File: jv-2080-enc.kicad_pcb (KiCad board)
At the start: 2 copper layers, 40 x 30 mm, 9 parts, among them J1 Conn_01x04, SW1 RotaryEncoder_Switch, U1 ATtiny13A-P

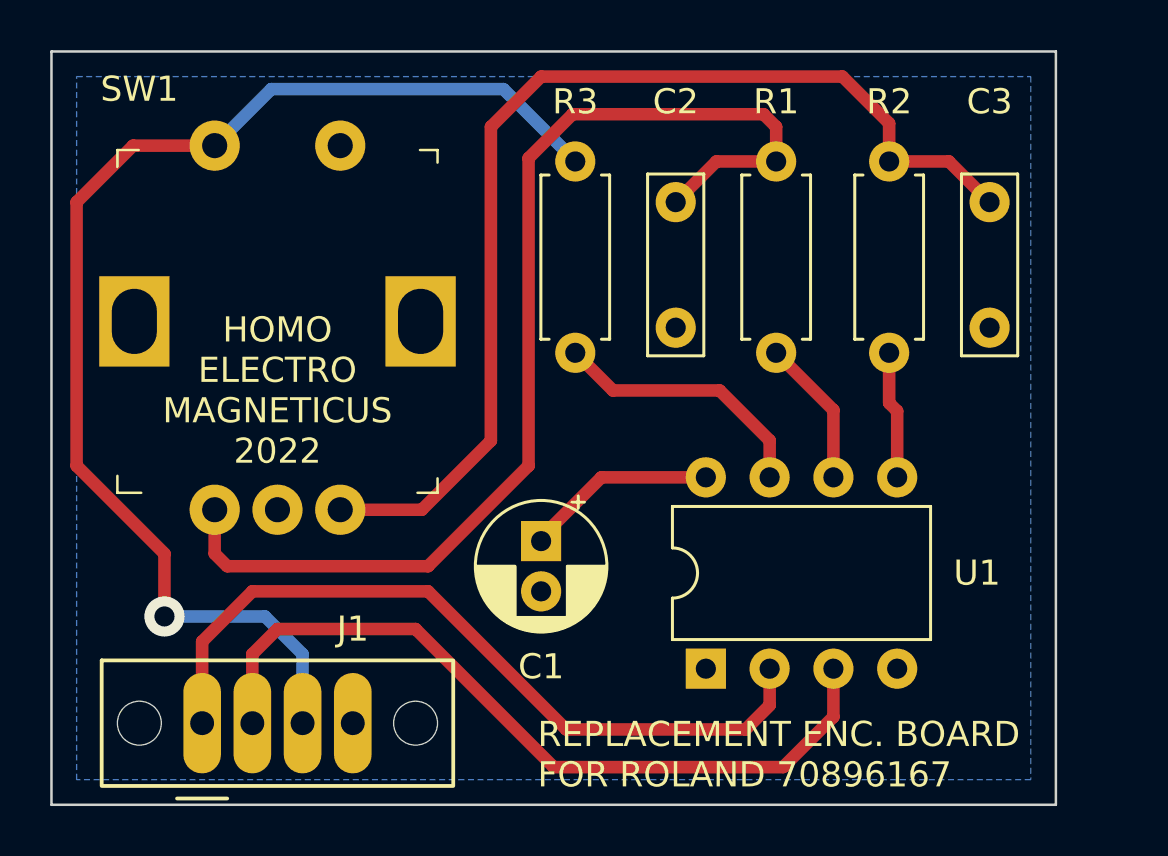
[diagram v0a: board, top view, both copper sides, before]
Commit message: Rounding all the tracks and adding teardrops for fun.
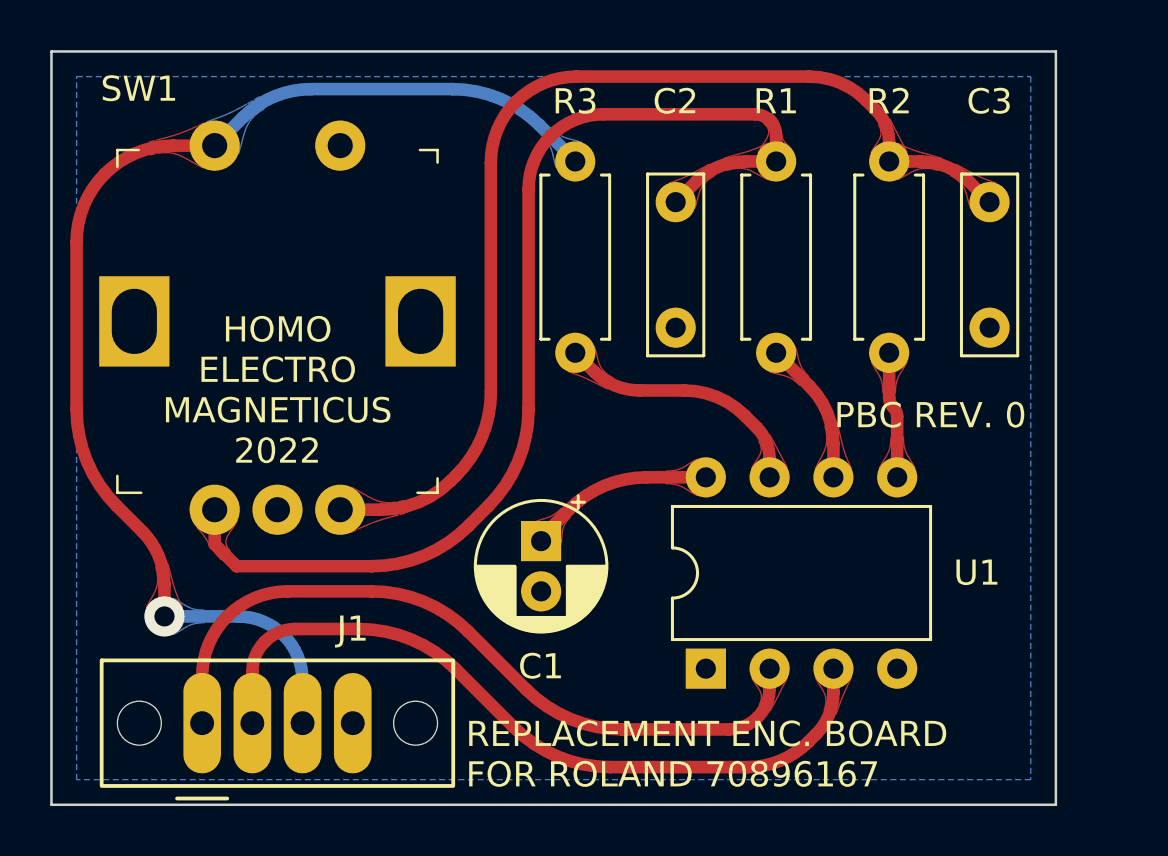
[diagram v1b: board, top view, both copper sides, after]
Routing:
- net Net-(C2-Pad1): track 45.5 -> 43.8 mm
- net Net-(C3-Pad1): track 43.3 -> 41.8 mm
- net /SWITCH: track 49.7 -> 48.3 mm
- net /ENC_A_OUT: track 30.8 -> 29.8 mm
- net /ENC_B_OUT: track 31.3 -> 30.4 mm
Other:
- board text added: "PBC REV. 0"

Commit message: Moved most of the components to the other side of the PCBA to account for the much smaller body size of a modern encoder vs the original one.
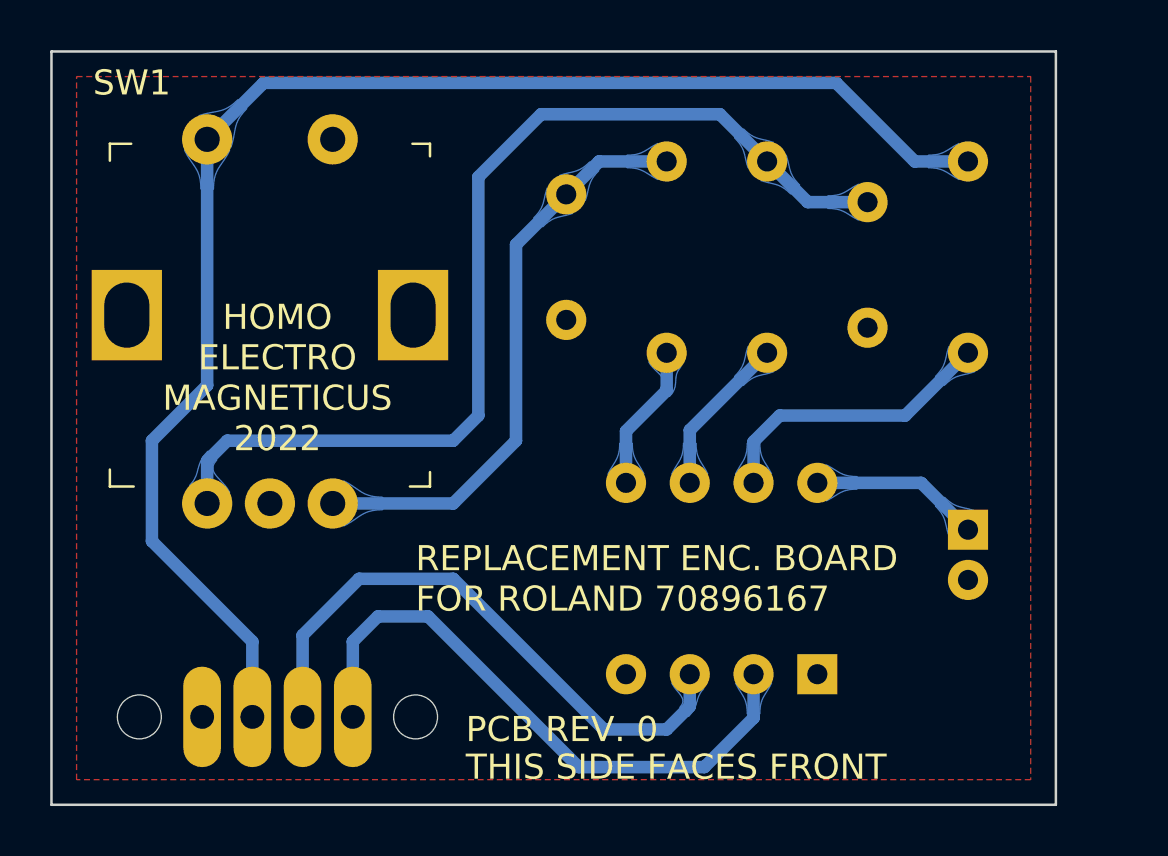
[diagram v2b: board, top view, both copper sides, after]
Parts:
- C1, C2, C3, J1, R1, R2, R3, U1: moved to B.Cu
- moved C1 17.0 mm to (158.5, 103.0)
- moved C3 16.9 mm to (142.5, 89.7)
- moved R3 15.6 mm to (158.5, 96.0)
- moved R2 8.86 mm to (146.5, 96.0)
- moved C2 7.64 mm to (154.5, 90.0)
- moved J1 6.01 mm to (134.0, 110.5), turned to 180 degrees
- moved U1 4.45 mm to (152.5, 108.8)
- moved SW1 0.39 mm to (125.0, 94.5)
- moved R1 0.36 mm to (150.5, 96.0)
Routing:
- net Net-(C3-Pad1): track 41.8 -> 23.5 mm
- net /SWITCH: track 48.3 -> 58.1 mm, vias 1 -> 0
- net /ENC_B_OUT: track 30.4 -> 23.7 mm
- net /ENC_A_OUT: track 29.8 -> 24.4 mm
- net Net-(C2-Pad1): track 43.8 -> 40.7 mm
- net Net-(R3-Pad1): track 10.3 -> 11.6 mm
- net /ENC_B_IN: track 5.04 -> 5.85 mm
- net Net-(C1-Pad1): track 7.54 -> 6.77 mm
- net /ENC_A_IN: track 5.75 -> 6.46 mm
- added copper zone on F.Cu, net GND
- removed copper zone on B.Cu, net GND
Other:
- board text added: "PCB REV. 0"
- board text added: "THIS SIDE FACES FRONT"
- board text removed: "PBC REV. 0"

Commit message: Re-drew the schematic to be easier to read. Tweaked the layout so that the PCB is 2mm less wide.
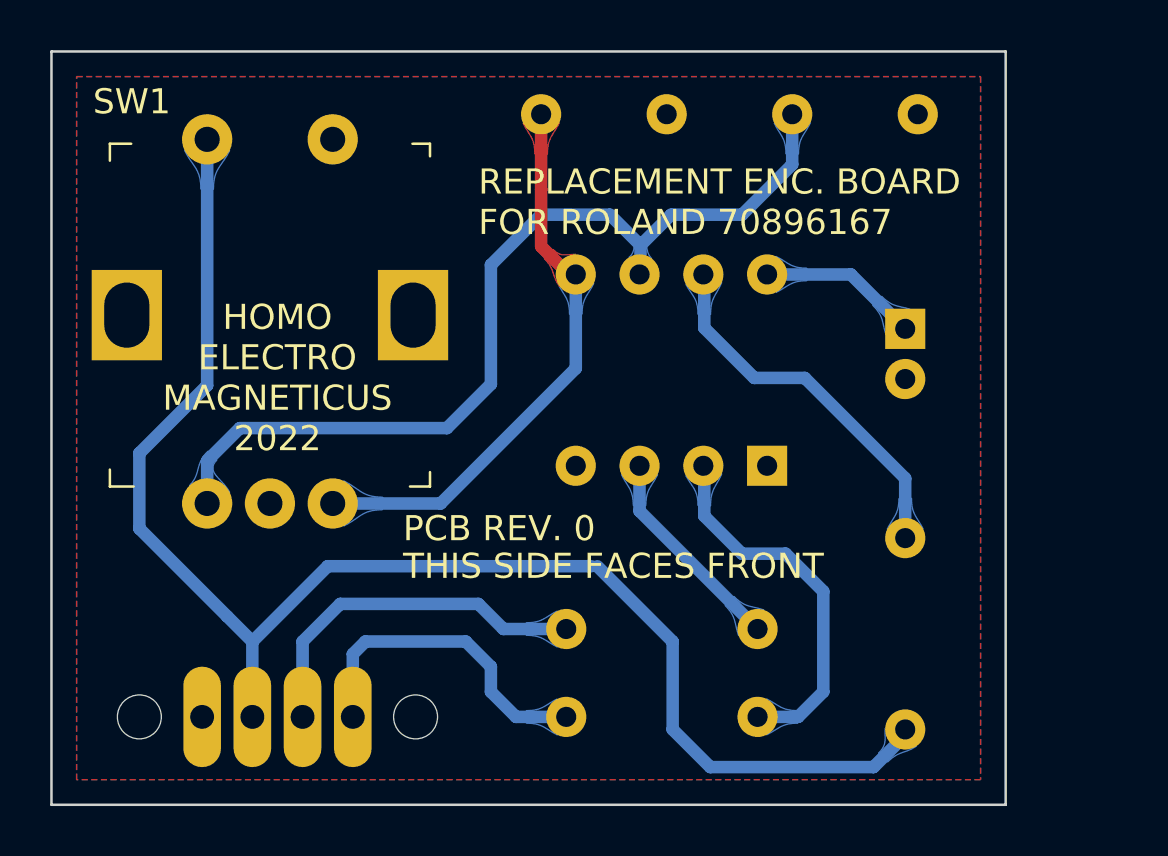
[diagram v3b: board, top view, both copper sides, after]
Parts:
- moved R1 16.6 mm to (142.5, 110.5), turned to 0 degrees
- moved R3 15.2 mm to (156.0, 111.0)
- moved R2 11.7 mm to (142.5, 107.0), turned to 0 degrees
- moved U1 8.54 mm to (150.5, 100.5)
- moved C1 8.38 mm to (156.0, 95.0)
- moved C2 4.61 mm to (151.5, 86.5), turned to 0 degrees
- moved C3 3.34 mm to (141.5, 86.5), turned to 0 degrees
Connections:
- C2 pad 1: Net-(C2-Pad1) -> /ENC_A_IN
- C3 pad 1: Net-(C3-Pad1) -> /ENC_B_IN
- J1 pad 1: /ENC_A_OUT -> Net-(J1-Pad1)
- J1 pad 2: /ENC_B_OUT -> Net-(J1-Pad2)
- R1 pad 1: /ENC_A_IN -> Net-(J1-Pad1)
- R1 pad 2: Net-(C2-Pad1) -> /ENC_A_OUT
- R2 pad 1: /ENC_B_IN -> Net-(J1-Pad2)
- R2 pad 2: Net-(C3-Pad1) -> /ENC_B_OUT
- R3 pad 1: Net-(R3-Pad1) -> /SWITCH
- R3 pad 2: /SWITCH -> /SWITCH_IN
- SW1 pad A: Net-(C2-Pad1) -> /ENC_A_IN
- SW1 pad B: Net-(C3-Pad1) -> /ENC_B_IN
- U1 pad 7: Net-(R3-Pad1) -> /SWITCH_IN
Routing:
- net Net-(C2-Pad1): track 40.7 -> 0.00 mm
- net /ENC_A_IN: track 6.46 -> 36.9 mm
- net Net-(C3-Pad1): track 23.5 -> 0.00 mm
- net /ENC_B_IN: track 5.85 -> 22.9 mm
- net /ENC_B_OUT: track 23.7 -> 8.45 mm
- net /SWITCH_IN: track 0.00 -> 14.7 mm
- net Net-(J1-Pad2): track 0.00 -> 14.5 mm
- net Net-(J1-Pad1): track 0.00 -> 13.0 mm
- net Net-(R3-Pad1): track 11.6 -> 0.00 mm
- net /ENC_A_OUT: track 24.4 -> 14.3 mm
- net /SWITCH: track 58.1 -> 59.2 mm
- added copper zone on B.Cu, net GND
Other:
- board size 40 x 30 mm -> 38 x 30 mm
- board text added: "0.5000 mm / 0.2500 mm"
- board text added: "38.0000 mm x 30.0000 mm"
- board text removed: "0.5000 mm / 0.2000 mm"
- board text removed: "40.0000 mm x 30.0000 mm"
